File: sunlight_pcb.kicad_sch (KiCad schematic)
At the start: 26 parts, among them J1 Conn_01x01, J2 Conn_01x01, J3 Conn_01x01, J4 Conn_01x01, J5 NTC, J6 PJ-036AH-SMT-TR, J7 Conn_01x02, Q1 DMN63D8LW, Q2 DMN63D8LW, U1 LDH-65-700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

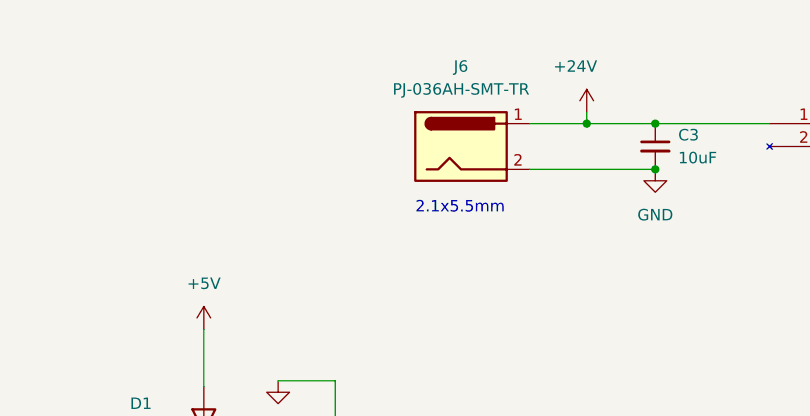
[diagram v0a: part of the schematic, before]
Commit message: change barrel to tht and update 3d models
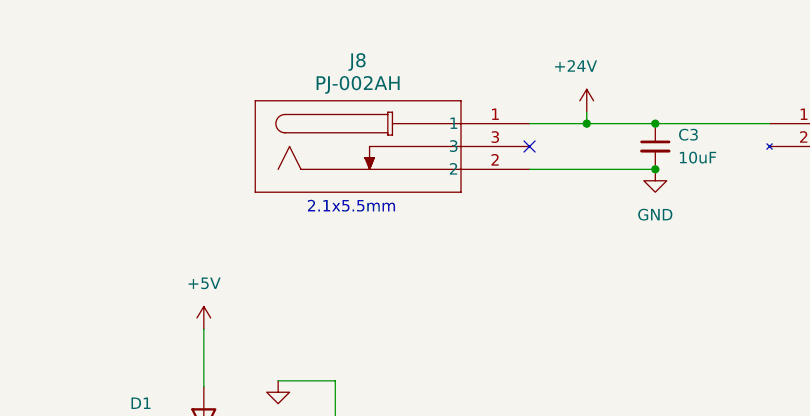
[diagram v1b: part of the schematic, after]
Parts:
- removed J6: PJ-036AH-SMT-TR, Connector_BarrelJack:BarrelJack_CUI_PJ-036AH-SMT_Horizontal, symbol Connector:Barrel_Jack
- added J8: PJ-002AH, sunlight_pcb:CUI_PJ-002AH, symbol sunlight_pcb:PJ-002AH
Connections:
- net +24V: now also J8.1
- net GND: now also J8.2
- no-connect marks 10 -> 11
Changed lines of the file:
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@@
   )
   (no_connect (at 78.74 87.63))
+  (no_connect (at 85.09 45.72))
   (no_connect (at 67.31 87.63))
   (no_connect (at 92.71 110.49))
@@
     (effects (font (size 1.27 1.27)) (justify left bottom))
   )
-  (text "2.1x5.5mm" (at 72.39 53.34 0)
+  (text "2.1x5.5mm" (at 60.325 53.34 0)
     (effects (font (size 1.27 1.27)) (justify left bottom))
   )
@@
     )
   )
+  (symbol (lib_id "sunlight_pcb:PJ-002AH") (at 85.09 43.18 0) (unit 1)
+    (in_bom yes) (on_board yes) (dnp no) (fields_autoplaced)
+    (property "Reference" "J8" (at 66.04 36.195 0)
+      (effects (font (size 1.524 1.524)))
+    )
+    (property "Value" "PJ-002AH" (at 66.04 38.735 0)
+      (effects (font (size 1.524 1.524)))
+    )
+    (property "Footprint" "sunlight_pcb:CUI_PJ-002AH" (at 87.63 38.1 0)
+      (effects (font (size 1.27 1.27) italic) hide)
+    )
+    (property "Datasheet" "PJ-002AH" (at 87.63 40.64 0)
+      (effects (font (size 1.27 1.27) italic) hide)
+    )
+    (pin "1")
+    (pin "2")
+    (pin "3")
+    (instances
+      (project "sunlight_pcb"
+        (path "/cb240cfb-11bb-4578-a6ce-a04e069b00ef"
+          (reference "J8") (unit 1)
+        )
+      )
+    )
+  )
   (symbol (lib_id "Device:C_Small") (at 99.06 45.72 0) (unit 1)
     (in_bom yes) (on_board yes) (dnp no) (fields_autoplaced)
@@
         )
       )
-    )
-  )
-  (symbol (lib_id "Connector:Barrel_Jack") (at 77.47 45.72 0) (unit 1)
-    (in_bom yes) (on_board yes) (dnp no) (fields_autoplaced)
-    (property "Reference" "J6" (at 77.47 36.83 0)
-      (effects (font (size 1.27 1.27)))
-    )
-    (property "Value" "PJ-036AH-SMT-TR\n" (at 77.47 39.37 0)
-      (effects (font (size 1.27 1.27)))
-    )
-    (property "Footprint" "Connector_BarrelJack:BarrelJack_CUI_PJ-036AH-SMT_Horizontal" (at 78.74 46.736 0)
-      (effects (font (size 1.27 1.27)) hide)
-    )
-    (property "Datasheet" "~" (at 78.74 46.736 0)
-      (effects (font (size 1.27 1.27)) hide)
-    )
-    (pin "1")
-    (pin "2")
-    (instances
-      (project "sunlight_pcb"
-        (path "/cb240cfb-11bb-4578-a6ce-a04e069b00ef"
-          (reference "J6") (unit 1)
-        )
-      )

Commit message: layout done, gerbers gened
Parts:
- C9: footprint Capacitor_SMD:C_0402_1005Metric -> Capacitor_SMD:C_0603_1608Metric_Pad1.08x0.95mm_HandSolder
- D1, R2, R3: footprint (none) -> Diode_SMD:D_0603_1608Metric_Pad1.05x0.95mm_HandSolder
- J1, J2, J3, J4: footprint Connector_Wire:SolderWire-0.5sqmm_1x01_D0.9mm_OD2.1mm -> Connector_Wire:SolderWire-2sqmm_1x01_D2mm_OD3.9mm
- J5: footprint O32controller:SolderNTC-1.27mm -> sunlight_pcb:SolderNTC-1.27mm
- J7: footprint (none) -> Connector_PinHeader_2.54mm:PinHeader_1x02_P2.54mm_Vertical
- R7: footprint Resistor_SMD:R_0402_1005Metric -> Resistor_SMD:R_0603_1608Metric_Pad0.98x0.95mm_HandSolder
- TP1, TP2, TP3, TP4: footprint (none) -> TestPoint:TestPoint_Pad_1.0x1.0mm
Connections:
- net +3.3V is gone; now on net +3V3: J5.1 (Pin_1)
- net +3V3: now also U3.12 (3V3)
- net BLUE_INPUT: now also U3.8 (PB09_A7_D7_RX); no longer U3.6 (PA9_A5_D5_SCL)
- net GND: now also J8.3
- net UART_RX: now also U3.2 (PA4_A1_D1); no longer U3.8 (PB09_A7_D7_RX)
- net UART_TX: now also U3.3 (PA10_A2_D2); no longer U3.7 (PB08_A6_D6_TX)
- net at C9.1, J5.2 (Pin_2), R7.2: now also U3.4 (PA11_A3_D3); no longer U3.1 (PA02_A0_D0)
- no-connect marks 11 -> 12
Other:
- moved on the sheet: C9, J5, J7, R7
